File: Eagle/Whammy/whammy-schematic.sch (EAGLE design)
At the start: 7 parts, among them J1 POWER_JACK

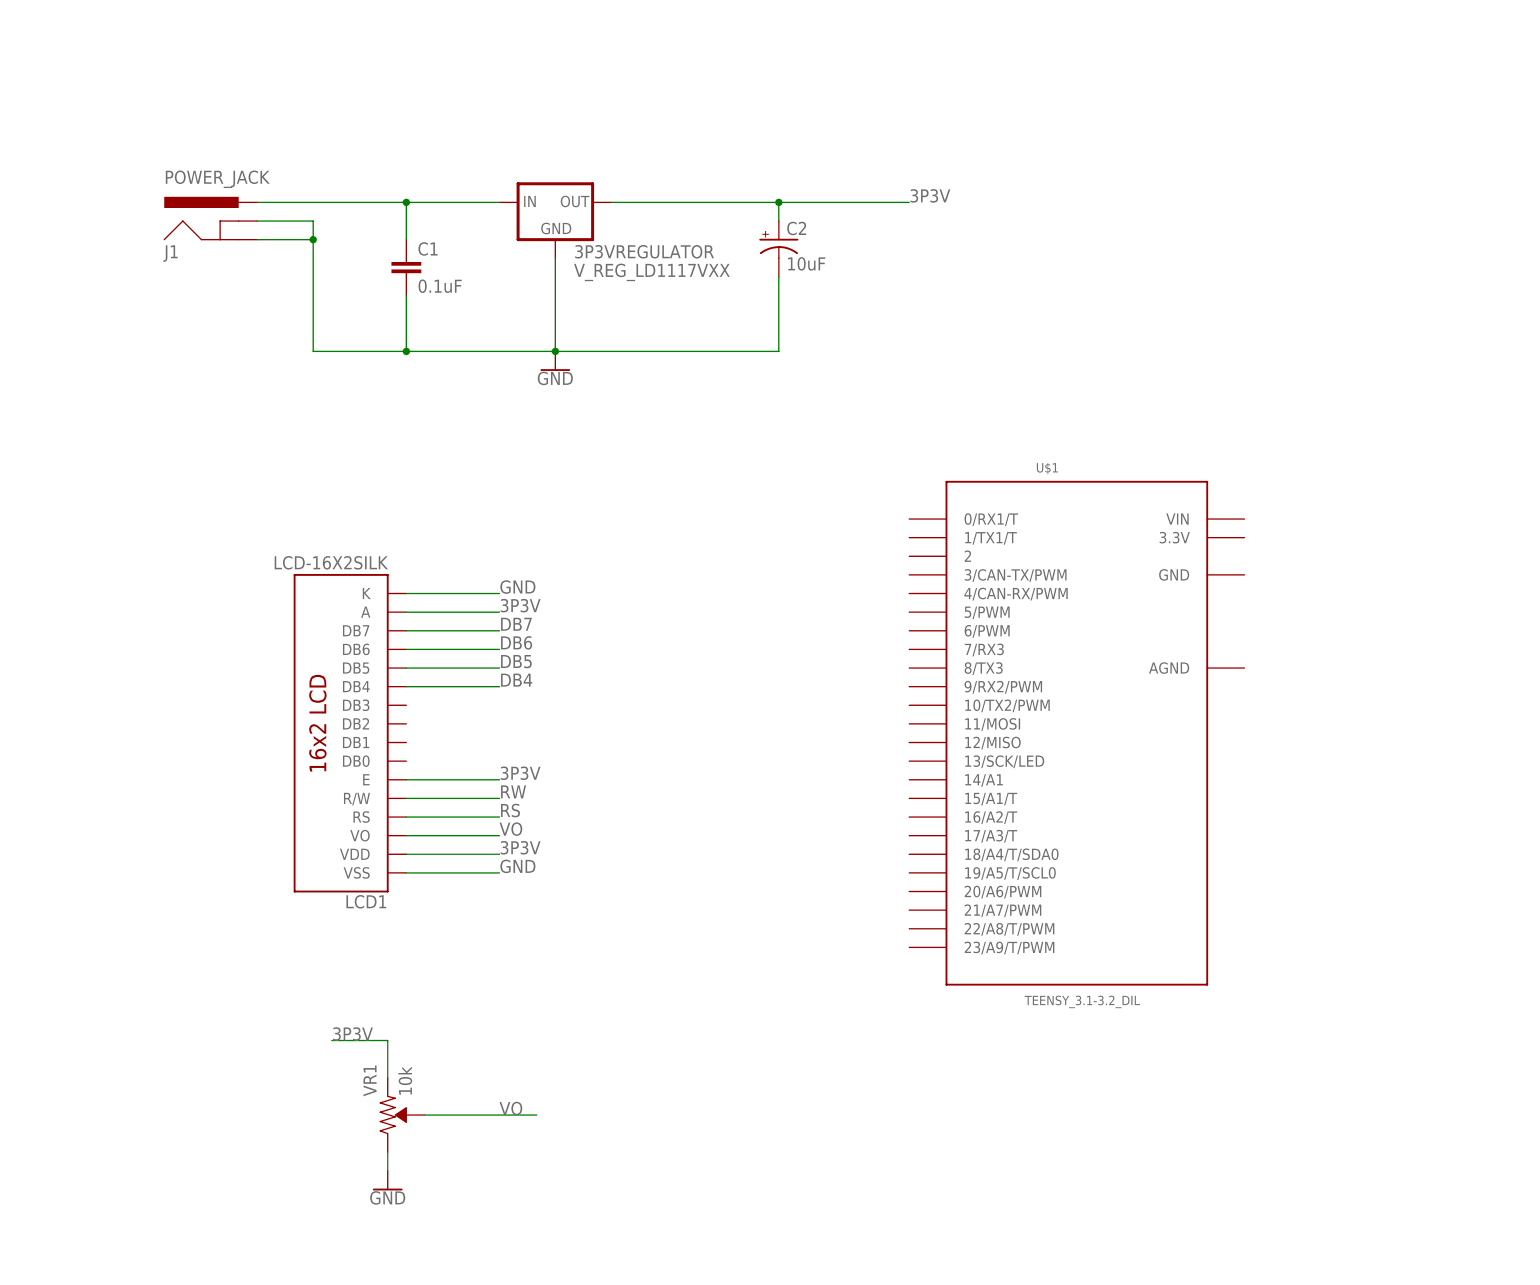
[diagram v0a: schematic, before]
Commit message: First version of schematic.
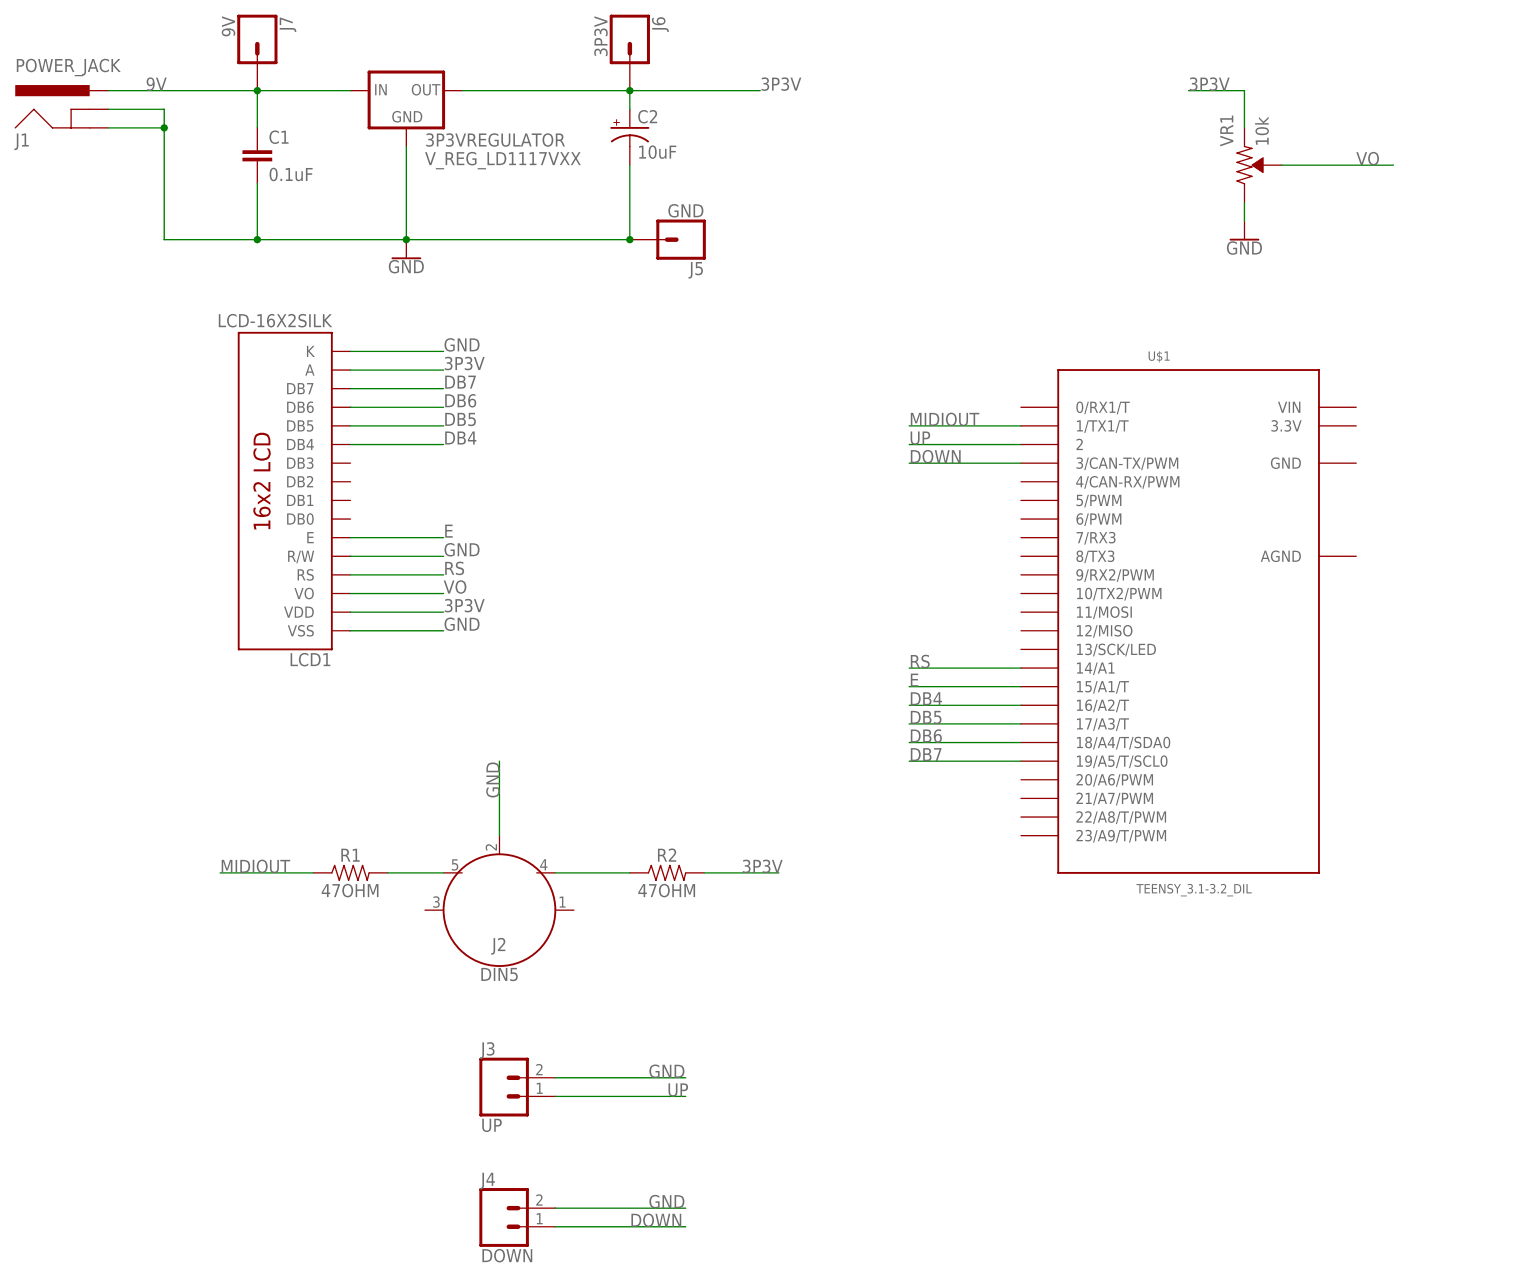
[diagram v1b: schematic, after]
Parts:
- added J2: DIN5, SparkFun-Connectors:DIN5
- added J3: UP, SparkFun-Connectors:CONN_02
- added J4: DOWN, SparkFun-Connectors:CONN_02
- added J5: GND, SparkFun-Connectors:CONN_01
- added J6: 3P3V, SparkFun-Connectors:CONN_01
- added J7: 9V, SparkFun-Connectors:CONN_01
- added R1, R2: 47OHM, SparkFun-Resistors:RESISTORAXIAL-0.3-KIT
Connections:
- removed net RW: LCD1.R/W
- new net 9V: 3P3VREGULATOR.IN, C1.1, J1.PWR, J7.1
- new net DOWN: J4.1, U$1.3/CAN-TX/PWM
- new net E: LCD1.E, U$1.15/A1/T
- new net MIDIOUT: R1.1, U$1.1/TX1/T
- new net N$2: J2.4, R2.1
- new net UP: J3.1, U$1.2
- net 3P3V: now also J6.1, R2.2; no longer LCD1.E
- net DB4: now also U$1.16/A2/T
- net DB5: now also U$1.17/A3/T
- net DB6: now also U$1.18/A4/T/SDA0
- net DB7: now also U$1.19/A5/T/SCL0
- net GND: now also J2.2, J3.2, J4.2, J5.1, LCD1.R/W
- net N$1: now also J2.5, R1.2; no longer 3P3VREGULATOR.IN, C1.1, J1.PWR
- net RS: now also U$1.14/A1
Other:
- moved on the sheet: 3P3VREGULATOR, C1, C2, J1, LCD1, U$1, VR1

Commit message: Schematic and layout started.
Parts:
- removed 3P3VREGULATOR: V_REG_LD1117VXX, SparkFun-IC-Power:V_REG_LD1117VXX
- added J8: 3P3V, SparkFun-Connectors:CONN_01
- added U1: 5V REGULATOR, SparkFun-IC-Power:V_REG_78XX-TO-220
- C1: value 0.1uF -> 0.33uF
- C2: value 10uF -> 0.1uF
- J6: value 3P3V -> 5V
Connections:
- new net 5V: C2.+, J6.1, LCD1.A, LCD1.VDD, U$1.VIN, U1.OUT, VR1.CCW
- net 3P3V: now also J8.1, U$1.3.3V; no longer 3P3VREGULATOR.OUT, C2.+, J6.1, LCD1.A, LCD1.VDD, VR1.CCW
- net 9V: now also U1.IN; no longer 3P3VREGULATOR.IN
- net GND: now also U$1.AGND, U$1.GND, U1.GND; no longer 3P3VREGULATOR.GND

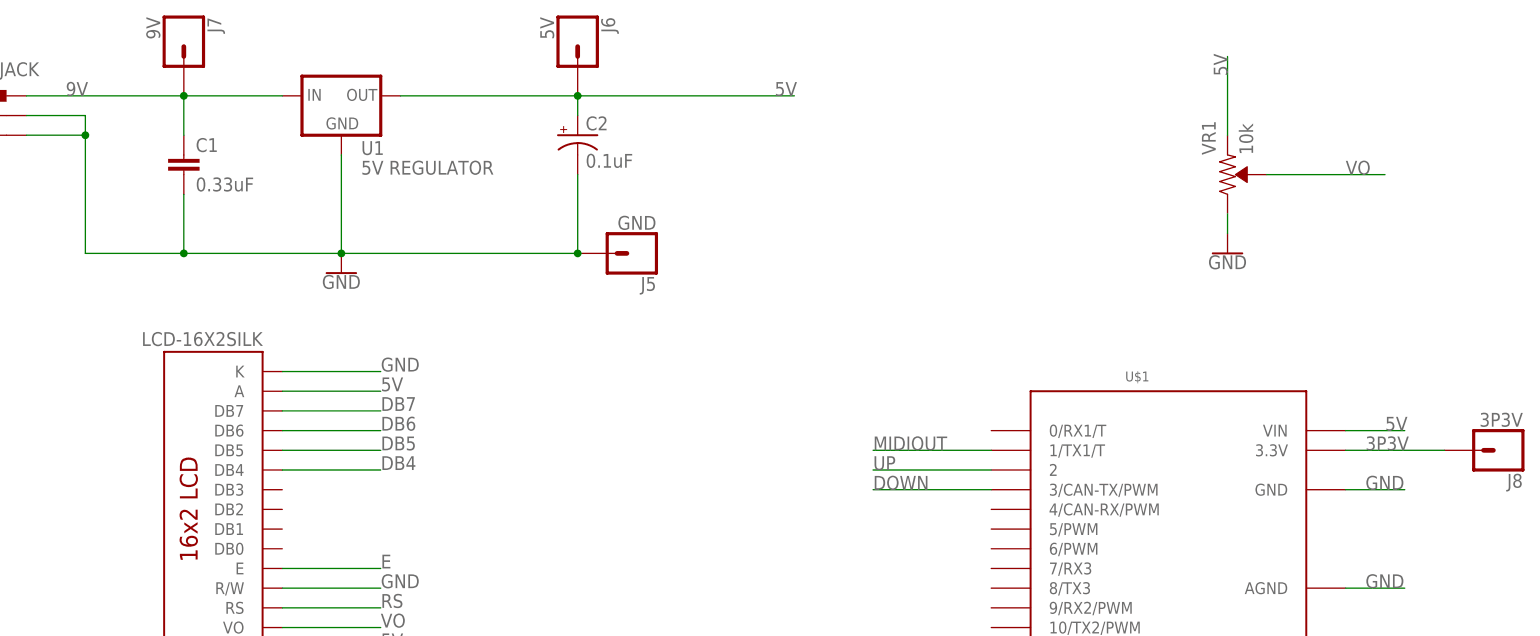
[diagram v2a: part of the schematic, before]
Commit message: Added initial layout. No ground fill yet.
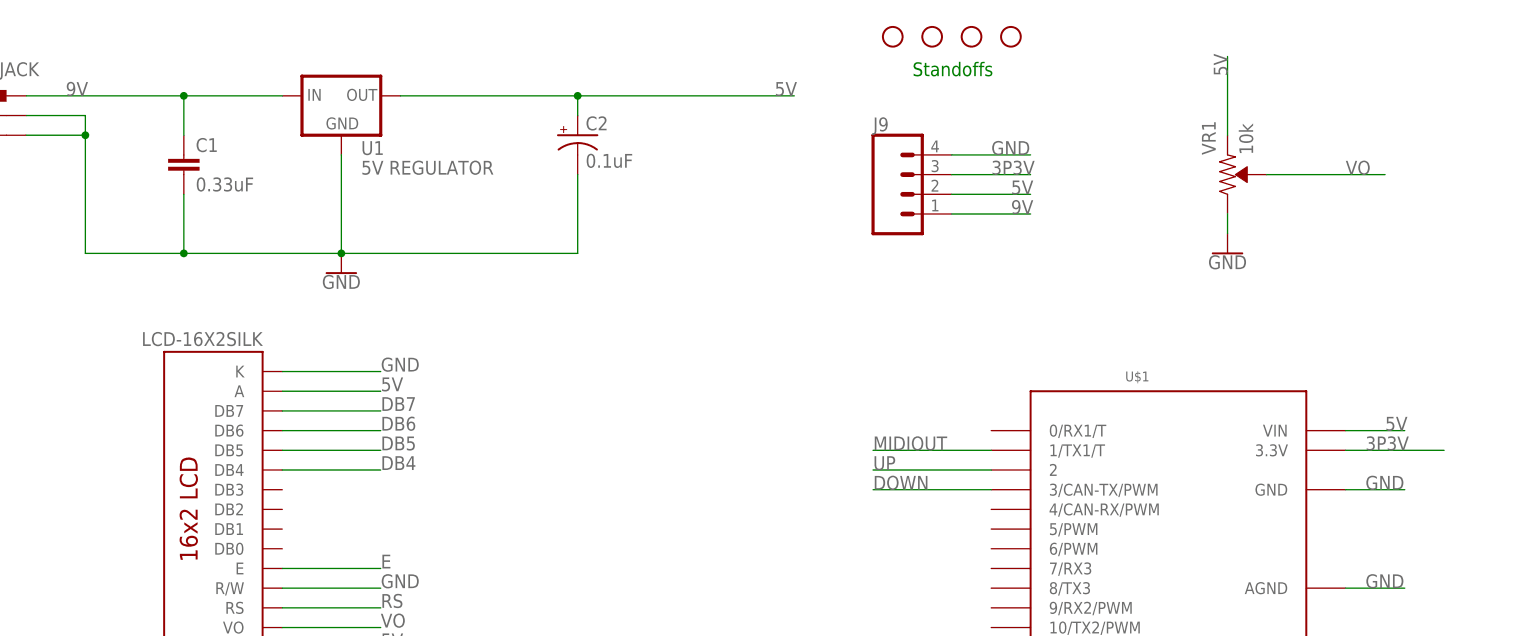
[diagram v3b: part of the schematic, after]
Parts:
- removed J5: GND, SparkFun-Connectors:CONN_01
- removed J6: 5V, SparkFun-Connectors:CONN_01
- removed J7: 9V, SparkFun-Connectors:CONN_01
- removed J8: 3P3V, SparkFun-Connectors:CONN_01
- added H1, H2, H3, H4: STAND-OFF, SparkFun-Hardware:STAND-OFF
- added J9: (no value), SparkFun-Connectors:CONN_04
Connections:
- net 3P3V: now also J9.3; no longer J8.1
- net 5V: now also J9.2; no longer J6.1
- net 9V: now also J9.1; no longer J7.1
- net GND: now also J9.4; no longer J5.1
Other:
- note added: "Standoffs"
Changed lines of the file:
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@@
 <part name="R1" library="SparkFun-Resistors" deviceset="RESISTOR" device="AXIAL-0.3-KIT" value=" 47OHM"/>
 <part name="R2" library="SparkFun-Resistors" deviceset="RESISTOR" device="AXIAL-0.3-KIT" value=" 47OHM"/>
-<part name="J5" library="SparkFun-Connectors" deviceset="CONN_01" device="" value="GND"/>
-<part name="J6" library="SparkFun-Connectors" deviceset="CONN_01" device="" value="5V"/>
-<part name="J7" library="SparkFun-Connectors" deviceset="CONN_01" device="" value="9V"/>
 <part name="J3" library="SparkFun-Connectors" deviceset="CONN_02" device="" value="UP"/>
 <part name="J4" library="SparkFun-Connectors" deviceset="CONN_02" device="" value="DOWN"/>
 <part name="U1" library="SparkFun-IC-Power" deviceset="V_REG_78XX" device="-TO-220" value="5V REGULATOR"/>
-<part name="J8" library="SparkFun-Connectors" deviceset="CONN_01" device="" value="3P3V"/>
+<part name="H1" library="SparkFun-Hardware" deviceset="STAND-OFF" device=""/>
+<part name="H2" library="SparkFun-Hardware" deviceset="STAND-OFF" device=""/>
+<part name="H3" library="SparkFun-Hardware" deviceset="STAND-OFF" device=""/>
+<part name="H4" library="SparkFun-Hardware" deviceset="STAND-OFF" device=""/>
+<part name="J9" library="SparkFun-Connectors" deviceset="CONN_04" device=""/>
 </parts>
 <sheets>
 <sheet>
 <plain>
+<text x="93.98" y="137.16" size="1.778" layer="91">Standoffs</text>
 </plain>
 <instances>
@@
 <instance part="R1" gate="G$1" x="12.7" y="27.94"/>
 <instance part="R2" gate="G$1" x="55.88" y="27.94"/>
-<instance part="J5" gate="G$1" x="58.42" y="114.3" rot="R180"/>
-<instance part="J6" gate="G$1" x="50.8" y="142.24" rot="R270"/>
-<instance part="J7" gate="G$1" x="0" y="142.24" rot="R270"/>
 <instance part="J3" gate="G$1" x="33.02" y="-2.54"/>
 <instance part="J4" gate="G$1" x="33.02" y="-20.32"/>
 <instance part="U1" gate="G$1" x="20.32" y="134.62"/>
-<instance part="J8" gate="G$1" x="170.18" y="88.9" rot="R180"/>
+<instance part="H1" gate="G$1" x="91.44" y="142.24"/>
+<instance part="H2" gate="G$1" x="96.52" y="142.24"/>
+<instance part="H3" gate="G$1" x="101.6" y="142.24"/>
+<instance part="H4" gate="G$1" x="106.68" y="142.24"/>
+<instance part="J9" gate="G$1" x="93.98" y="121.92"/>
 </instances>
 <busses>
@@
 <junction x="0" y="134.62"/>
 <label x="-15.24" y="134.62" size="1.778" layer="95"/>
-<pinref part="J7" gate="G$1" pin="1"/>
 <pinref part="U1" gate="G$1" pin="IN"/>
+</segment>
+<segment>
+<pinref part="J9" gate="G$1" pin="1"/>
+<wire x1="99.06" y1="119.38" x2="109.22" y2="119.38" width="0.1524" layer="91"/>
+<label x="106.68" y="119.38" size="1.778" layer="95"/>
 </segment>
 </net>
@@
 <wire x1="50.8" y1="124.46" x2="50.8" y2="114.3" width="0.1524" layer="91"/>
 <wire x1="50.8" y1="114.3" x2="20.32" y2="114.3" width="0.1524" layer="91"/>
-<pinref part="J5" gate="G$1" pin="1"/>
-<junction x="50.8" y="114.3"/>
 <pinref part="U1" gate="G$1" pin="GND"/>
 </segment>
@@
 <wire x1="149.86" y1="71.12" x2="157.48" y2="71.12" width="0.1524" layer="91"/>
 <label x="152.4" y="71.12" size="1.778" layer="95"/>
+</segment>
+<segment>
+<pinref part="J9" gate="G$1" pin="4"/>
+<wire x1="99.06" y1="127" x2="109.22" y2="127" width="0.1524" layer="91"/>
+<label x="104.14" y="127" size="1.778" layer="95"/>
 </segment>
 </net>
@@
 <wire x1="50.8" y1="134.62" x2="50.8" y2="132.08" width="0.1524" layer="91"/>
 <junction x="50.8" y="134.62"/>
-<pinref part="J6" gate="G$1" pin="1"/>
 <pinref part="U1" gate="G$1" pin="OUT"/>
 <wire x1="50.8" y1="134.62" x2="78.74" y2="134.62" width="0.1524" layer="91"/>
@@
 <label x="25.4" y="63.5" size="1.778" layer="95"/>
 </segment>
+<segment>
+<pinref part="J9" gate="G$1" pin="2"/>
+<wire x1="99.06" y1="121.92" x2="109.22" y2="121.92" width="0.1524" layer="91"/>
+<label x="106.68" y="121.92" size="1.778" layer="95"/>
+</segment>
 </net>
 <net name="3P3V" class="0">
@@
 <wire x1="149.86" y1="88.9" x2="162.56" y2="88.9" width="0.1524" layer="91"/>
 <label x="152.4" y="88.9" size="1.778" layer="95"/>
-<pinref part="J8" gate="G$1" pin="1"/>
 </segment>
 <segment>
@@
 <label x="68.58" y="27.94" size="1.778" layer="95"/>
 </segment>
-</net>
+<segment>
+<pinref part="J9" gate="G$1" pin="3"/>
+<wire x1="99.06" y1="124.46" x2="109.22" y2="124.46" width="0.1524" layer="91"/>
+<label x="104.14" y="124.46" size="1.778" layer="95"/>
+</segment>
+</net>
